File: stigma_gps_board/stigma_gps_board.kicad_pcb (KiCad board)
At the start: 2 copper layers, 40 x 40 mm, 22 parts, among them J1 Conn_02x05_Top_Bottom, U1 NCP115AMX120TCG, U2 SAM-M10Q

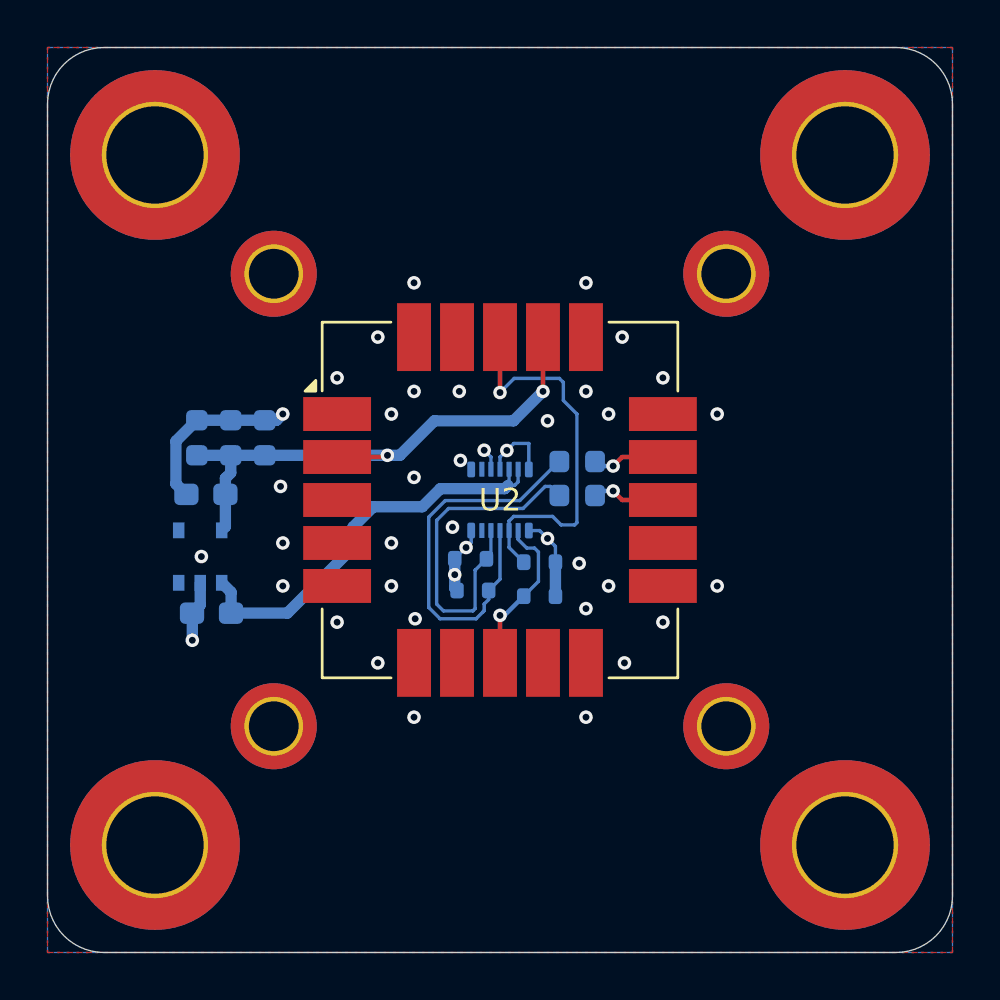
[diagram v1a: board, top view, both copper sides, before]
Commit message: Update GPS board for mission board
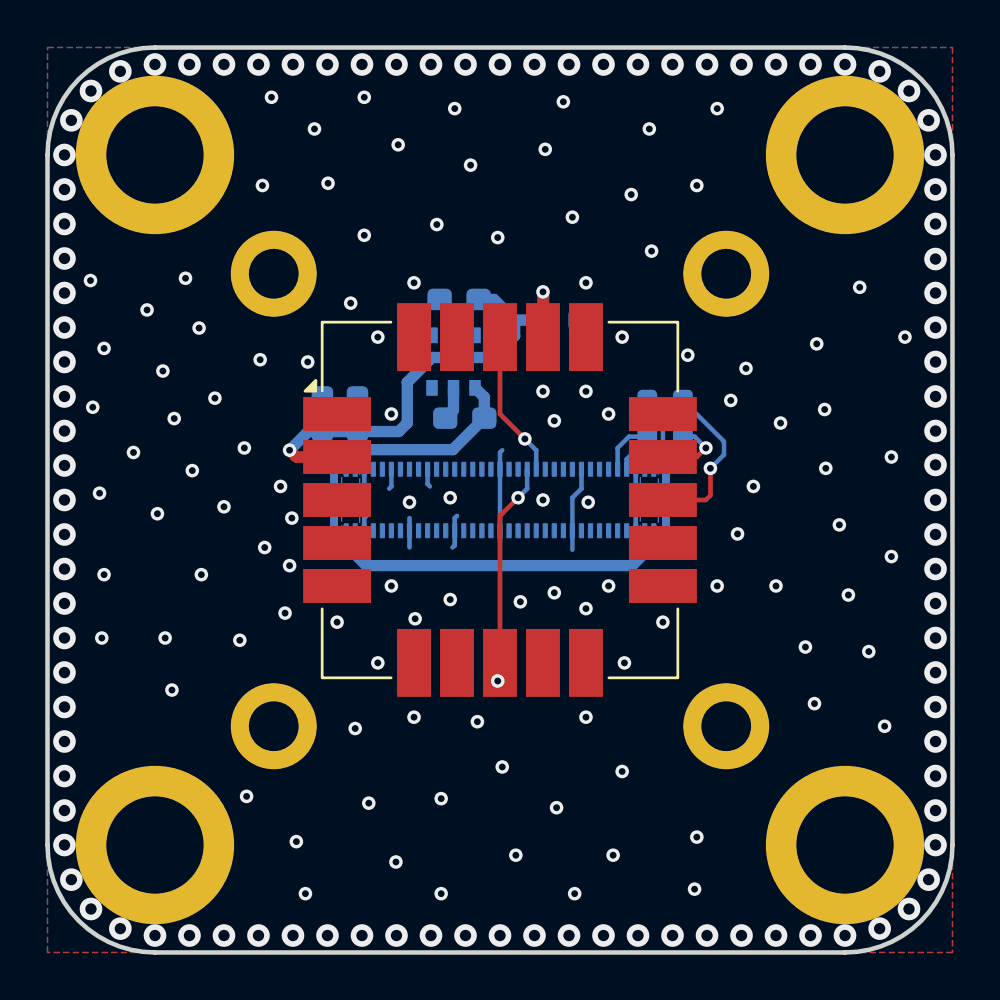
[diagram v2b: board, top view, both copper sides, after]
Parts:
- removed D1, D2, D3, D4: ESD5Zxx, Diode_SMD:D_SOD-523
- H1, H2, H3, H4: footprint MountingHole:MountingHole_2.2mm_M2_DIN965_Pad_TopBottom -> MountingHole:MountingHole_2.2mm_M2_ISO14580_Pad
- H5, H6, H7, H8: footprint MountingHole:MountingHole_4.3mm_M4_DIN965_Pad_TopBottom -> MountingHole:MountingHole_4.3mm_M4_ISO14580_Pad
- J1: value Conn_02x05_Top_Bottom -> DF40GB-70DP-0.4V; footprint stigma:DF40GB-10DP-0.4V-plug -> stigma:DF40GB-70DP-0.4V-plug
- moved C5 16.9 mm to (122.7, 62.0), turned to 180 degrees
- moved C2 14.1 mm to (118.2, 61.1)
- moved U1 14.1 mm to (117.9, 63.9)
- moved C1 14.1 mm to (118.4, 66.4)
- moved L2 5.72 mm to (127.3, 65.6)
- moved C3 4.23 mm to (113.7, 66.2)
- moved C4 4.18 mm to (112.2, 66.2)
- moved L1 4.04 mm to (127.3, 67.2)
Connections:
- C1 pad 2: 5V -> +5V
- J1 pad 1: 5V -> +5V
- J1 pad 2: 5V -> +5V
- J1 pad 4: GND -> UART8_RX_GPS
- J1 pad 5: unconnected-(J1-Pin_5-Pad5) -> UART8_TX_GPS
- J1 pad 6: GPS_SAFEBOOT -> unconnected-(J1-Pin_6-Pad6)
- J1 pad 7: GPS_RESET -> unconnected-(J1-Pin_7-Pad7)
- J1 pad 8: UART2_TX -> unconnected-(J1-Pin_8-Pad8)
- J1 pad 9: UART2_RX -> GND
- L1 pad 2: UART2_TX -> UART8_TX_GPS
- L2 pad 2: UART2_RX -> UART8_RX_GPS
- U1 pad 1: 5V -> +5V
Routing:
- net +5V: track 0.00 -> 24.4 mm
- net 5V: track 18.4 -> 0.00 mm
- net UART2_TX: track 17.8 -> 0.00 mm
- net UART2_RX: track 15.7 -> 0.00 mm
- net GPS_RESET: track 17.4 -> 6.50 mm
- net UART8_RX_GPS: track 0.00 -> 4.57 mm
- net Net-(U2-TXD): track 3.25 -> 7.38 mm
- net UART8_TX_GPS: track 0.00 -> 2.46 mm
- net +3.3V: track 24.6 -> 22.5 mm
- net GPS_SAFEBOOT: track 7.24 -> 9.06 mm
- net GND: track 21.4 -> 19.8 mm, vias 40 -> 209
- added copper zone on B.Cu, net +5V
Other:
- outline, holes or cut-outs redrawn
- board text added: "rev 1"
